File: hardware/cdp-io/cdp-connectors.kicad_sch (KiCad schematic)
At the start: 1 part, among them J1 Conn_01x26_Pin

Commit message: A really small progress.
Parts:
- added J1: Conn_02x20_Odd_Even, Connector_IDC:IDC-Header_2x20_P2.54mm_Vertical, symbol Connector_Generic:Conn_02x20_Odd_Even
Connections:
- net GND: now also J1.39 (Pin_39), J1.4 (Pin_4)
- new net CLOCK: J1.1 (Pin_1)
- new net D0: J1.29 (Pin_29)
- new net D1: J1.27 (Pin_27)
- new net D2: J1.25 (Pin_25)
- new net D3: J1.23 (Pin_23)
- new net D4: J1.21 (Pin_21)
- new net D5: J1.19 (Pin_19)
- new net D6: J1.17 (Pin_17)
- new net D7: J1.15 (Pin_15)
- new net MA0: J1.32 (Pin_32)
- new net MA1: J1.30 (Pin_30)
- new net MA2: J1.28 (Pin_28)
- new net MA3: J1.26 (Pin_26)
- new net MA4: J1.24 (Pin_24)
- new net MA5: J1.22 (Pin_22)
- new net MA6: J1.20 (Pin_20)
- new net MA7: J1.18 (Pin_18)
- new net N0: J1.37 (Pin_37)
- new net N1: J1.35 (Pin_35)
- new net N2: J1.33 (Pin_33)
- new net Q: J1.7 (Pin_7)
- new net SC0: J1.11 (Pin_11)
- new net SC1: J1.9 (Pin_9)
- new net TPA: J1.14 (Pin_14)
- new net TPB: J1.16 (Pin_16)
- new net VCC: J1.2 (Pin_2), J1.31 (Pin_31)
- new net ~{CLEAR}: J1.5 (Pin_5)
- new net ~{DMA IN}: J1.6 (Pin_6)
- new net ~{DMA OUT}: J1.8 (Pin_8)
- new net ~{EF1}: J1.34 (Pin_34)
- new net ~{EF2}: J1.36 (Pin_36)
- new net ~{EF3}: J1.38 (Pin_38)
- new net ~{EF4}: J1.40 (Pin_40)
- new net ~{INTERRUPT}: J1.10 (Pin_10)
- new net ~{MRD}: J1.13 (Pin_13)
- new net ~{MWR}: J1.12 (Pin_12)
- new net ~{WAIT}: J1.3 (Pin_3)

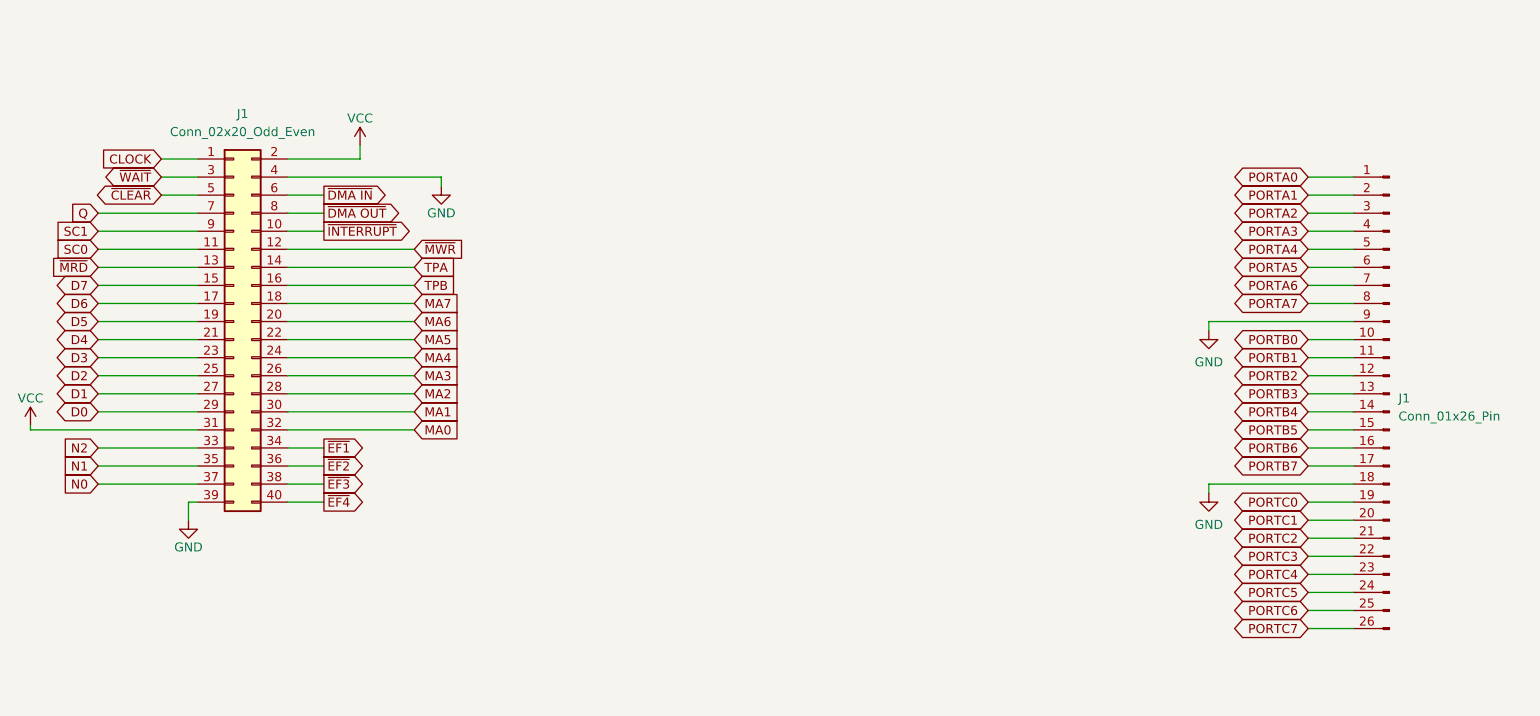
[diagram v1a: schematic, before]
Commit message: Renamed a few net, and changed the schematic a bit. The PCB is ready!
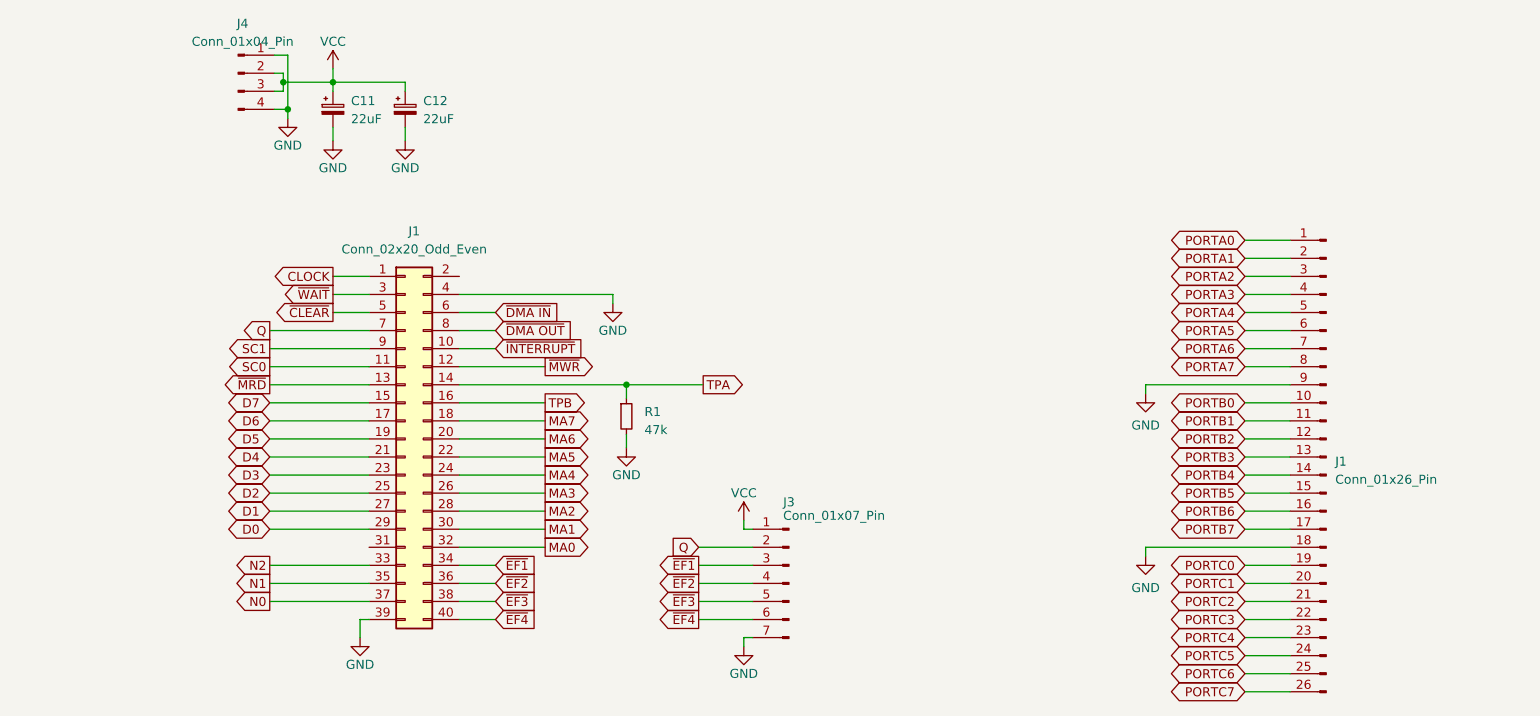
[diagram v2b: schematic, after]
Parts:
- added C11, C12: 22uF, Capacitor_THT:CP_Radial_D5.0mm_P2.00mm, symbol Device:C_Polarized_Small
- added J3: Conn_01x07_Pin, Connector_PinHeader_2.54mm:PinHeader_1x07_P2.54mm_Vertical, symbol Connector:Conn_01x07_Pin
- added J4: Conn_01x04_Pin, Connector_PinHeader_2.54mm:PinHeader_1x04_P2.54mm_Vertical, symbol Connector:Conn_01x04_Pin
- added R1: 47k, Resistor_THT:R_Axial_DIN0207_L6.3mm_D2.5mm_P10.16mm_Horizontal, symbol Device:R_Small
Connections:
- net GND: now also C11.2, C12.2, J3.7 (Pin_7), J4.1 (Pin_1), J4.4 (Pin_4), R1.2
- net Q: now also J3.2 (Pin_2)
- net TPA: now also R1.1
- net VCC: now also C11.1, C12.1, J3.1 (Pin_1), J4.2 (Pin_2), J4.3 (Pin_3); no longer J1.2 (Pin_2), J1.31 (Pin_31)
- net ~{EF1}: now also J3.3 (Pin_3)
- net ~{EF2}: now also J3.4 (Pin_4)
- net ~{EF3}: now also J3.5 (Pin_5)
- net ~{EF4}: now also J3.6 (Pin_6)
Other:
- moved on the sheet: J1

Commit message: The final version of the IO board. Gerber files added.
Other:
- company: (none) -> ZLED
- title: (none) -> Connectors
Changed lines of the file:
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@@
 (kicad_sch (version 20230121) (generator eeschema)
   (paper "A4")
+  (title_block
+    (title "Connectors")
+    (date "2023-07-06")
+    (rev "1")
+    (company "ZLED")
+  )
   (junction (at 77.47 43.18) (diameter 0) (color 0 0 0 0)
   )
